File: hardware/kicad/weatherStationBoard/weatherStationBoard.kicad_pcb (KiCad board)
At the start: 2 copper layers, 27 x 13 mm, 3 parts, among them P1 USB_C_Plug_USB2.0

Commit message: power, 5vto3v, usb to serial
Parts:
- added 12k1: R_Small, Resistor_SMD:R_0805_2012Metric, F.Cu at (100.6, 12.9)
- added C1: 100nF, Capacitor_SMD:C_0805_2012Metric, F.Cu at (91.8, 12.9)
- added C10: 100nF, Capacitor_SMD:C_0805_2012Metric, F.Cu at (96.2, 24.9)
- added C2: 10uF, Capacitor_SMD:C_0805_2012Metric, F.Cu at (91.8, 15.9)
- added C3: 22pF, Capacitor_SMD:C_0805_2012Metric, F.Cu at (91.8, 18.9)
- added C4: 22pF, Capacitor_SMD:C_0805_2012Metric, F.Cu at (91.8, 21.9)
- added C5: 100nF, Capacitor_SMD:C_0805_2012Metric, F.Cu at (91.8, 24.9)
- added C6: 100nF, Capacitor_SMD:C_0805_2012Metric, F.Cu at (96.2, 12.9)
- added C7: 10uF, Capacitor_SMD:C_0805_2012Metric, F.Cu at (96.2, 15.9)
- added C8: 100nF, Capacitor_SMD:C_0805_2012Metric, F.Cu at (96.2, 18.9)
- added C9: 10uF, Capacitor_SMD:C_0805_2012Metric, F.Cu at (96.2, 21.9)
- added D1: LED, LED_SMD:LED_0805_2012Metric, F.Cu at (91.8, 44.0)
- added Q1: S8050, Package_TO_SOT_THT:TO-92_Inline, F.Cu at (100.0, 29.7)
- added Q2: S8050, Package_TO_SOT_THT:TO-92_Inline, F.Cu at (100.0, 35.5)
- added R2: 470R, Resistor_SMD:R_0805_2012Metric, F.Cu at (100.6, 15.8)
- added R3: 470R, Resistor_SMD:R_0805_2012Metric, F.Cu at (100.6, 18.8)
- added R4: 1k, Resistor_SMD:R_0805_2012Metric, F.Cu at (100.6, 21.7)
- added R5: 12k, Resistor_SMD:R_0805_2012Metric, F.Cu at (100.6, 24.7)
- added U1: ESP-12F, RF_Module:ESP-12E, F.Cu at (80.0, 24.1)
- added U2: CH340G, Package_SO:SOIC-16_3.9x9.9mm_P1.27mm, F.Cu at (93.8, 32.4)
- added U4: AMS1117-3.3, Package_TO_SOT_SMD:SOT-223-3_TabPin2, F.Cu at (75.3, 42.0)
- added Y1: Crystal_GND24_Small, Crystal:Crystal_SMD_3225-4Pin_3.2x2.5mm, F.Cu at (92.2, 40.3)
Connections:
- net USB_VBUS_5V renamed 5V
- P1 pad A6: unconnected-(P1-D+-PadA6) -> Net-(P1-D+)
- P1 pad A7: unconnected-(P1-D--PadA7) -> Net-(P1-D-)
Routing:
- net 5V: track 0.00 -> 16.5 mm
- net Net-(D2-A): track 0.00 -> 5.65 mm
- net GND: track 0.00 -> 5.33 mm
- added copper zone on B.Cu, net GND
- added copper zone on F.Cu, net GND

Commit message: PCB updated
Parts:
- Q1, Q2: footprint Package_TO_SOT_THT:TO-92_Inline -> Package_TO_SOT_SMD:SOT-23-3
- moved U1 80.3 mm to (151.5, 60.5), turned to -90 degrees
- moved 12k1 61.8 mm to (133.1, 65.5)
- moved C6 60.5 mm to (145.5, 48.0)
- moved R2 57.8 mm to (112.0, 72.5)
- moved C7 54.3 mm to (140.0, 48.0)
- moved Y1 49.0 mm to (130.4, 70.8)
- moved U4 45.0 mm to (118.5, 54.5)
- moved C3 44.9 mm to (126.1, 47.8)
- moved C5 44.9 mm to (126.1, 53.8)
- moved R3 44.9 mm to (135.0, 47.6)
- moved R5 44.9 mm to (135.0, 53.5)
- moved C4 44.9 mm to (126.1, 50.8)
- moved R4 44.9 mm to (135.0, 50.5)
- moved C10 44.9 mm to (130.6, 53.8)
- moved C8 44.9 mm to (130.6, 47.8)
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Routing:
- net 5V: track 16.5 -> 8.07 mm
- net Net-(D2-A): track 5.65 -> 0.00 mm
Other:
- board size 27 x 13 mm -> 61 x 31 mm

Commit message: Updated usb connector
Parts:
- added R6: 5k1, Resistor_SMD:R_0805_2012Metric, F.Cu at (139.9, 28.3)
- added R7: 10k, Resistor_SMD:R_0805_2012Metric, F.Cu at (139.9, 31.3)
- added S1: PTS645SM43SMTR92LFS, PTS645SM43SMTR92LFS:PTS645_SMT_, F.Cu at (144.5, 23.2)
- P1: footprint Connector_USB:USB_C_Receptacle_GCT_USB4085 -> Connector_USB:USB_C_Receptacle_XKB_U262-16XN-4BVC11
- moved P1 3.41 mm to (106.6, 61.3)
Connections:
- P1 pad A5: unconnected-(P1-CC-PadA5) -> Net-(P1-CC)
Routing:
- net 5V: track 8.07 -> 0.00 mm
- net GND: track 5.33 -> 0.00 mm

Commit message: board design prototype no periphery
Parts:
- removed 12k1: R_Small, Resistor_SMD:R_0805_2012Metric
- removed P1: USB_C_Plug_USB2.0, Connector_USB:USB_C_Receptacle_XKB_U262-16XN-4BVC11
- added J1: USB_C_Receptacle_USB2.0_16P, Connector_USB:USB_C_Receptacle_XKB_U262-16XN-4BVC11, F.Cu at (108.2, 61.0)
- added R8: 5k1, Resistor_SMD:R_0805_2012Metric, F.Cu at (108.2, 68.2)
- added R9: 12k, Resistor_SMD:R_0805_2012Metric, F.Cu at (135.6, 74.0)
- moved R2 48.5 mm to (160.5, 72.0), turned to 90 degrees
- moved S1 42.7 mm to (109.0, 47.0), turned to -90 degrees
- moved R6 38.4 mm to (111.2, 54.0), turned to 180 degrees
- moved R3 36.9 mm to (162.7, 72.0), turned to 90 degrees
- moved C5 23.5 mm to (149.2, 49.8)
- moved C4 22.9 mm to (121.8, 73.2)
- moved C3 21.5 mm to (126.8, 69.2), turned to -90 degrees
- moved D2 19.5 mm to (115.8, 70.8), turned to 0 degrees
- moved R4 19.0 mm to (116.0, 49.5), turned to 180 degrees
- moved C6 19.0 mm to (127.5, 54.0)
- moved Q1 16.2 mm to (139.6, 70.2), turned to 180 degrees
- moved C1 15.5 mm to (129.5, 56.5)
- moved R1 15.1 mm to (115.8, 68.0), turned to 0 degrees
- moved R7 14.1 mm to (134.2, 44.2), turned to -90 degrees
- moved C2 14.1 mm to (129.5, 58.8)
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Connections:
- S1 pad 1: unconnected-(S1-Pad1) -> /nRST
- S1 pad 3: unconnected-(S1-Pad3) -> GND
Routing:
- net /nRST: track 0.00 -> 94.1 mm, vias 0 -> 6
- net Net-(U2-RXD): track 0.00 -> 71.9 mm, vias 0 -> 2
- net Net-(U2-TXD): track 0.00 -> 71.4 mm, vias 0 -> 2
- net 3V3: track 0.00 -> 48.8 mm, vias 0 -> 2
- net 5V: track 0.00 -> 46.5 mm
- net Net-(U2-V3): track 0.00 -> 40.1 mm, vias 0 -> 4
- net /DTR: track 0.00 -> 40.0 mm, vias 0 -> 2
- net /GPIO0: track 0.00 -> 35.3 mm, vias 0 -> 4
- net /RTS: track 0.00 -> 22.4 mm, vias 0 -> 4
- net /XI: track 0.00 -> 15.4 mm, vias 0 -> 2
- net Net-(U2-UD-): track 0.00 -> 13.8 mm, vias 0 -> 2
- net Net-(U2-UD+): track 0.00 -> 12.8 mm, vias 0 -> 2
- net /XO: track 0.00 -> 12.8 mm
- net Net-(Q1-B): track 0.00 -> 10.9 mm
- net Net-(J1-CC2): track 0.00 -> 10.3 mm, vias 0 -> 2
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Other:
- board size 61 x 31 mm -> 68.5 x 41 mm

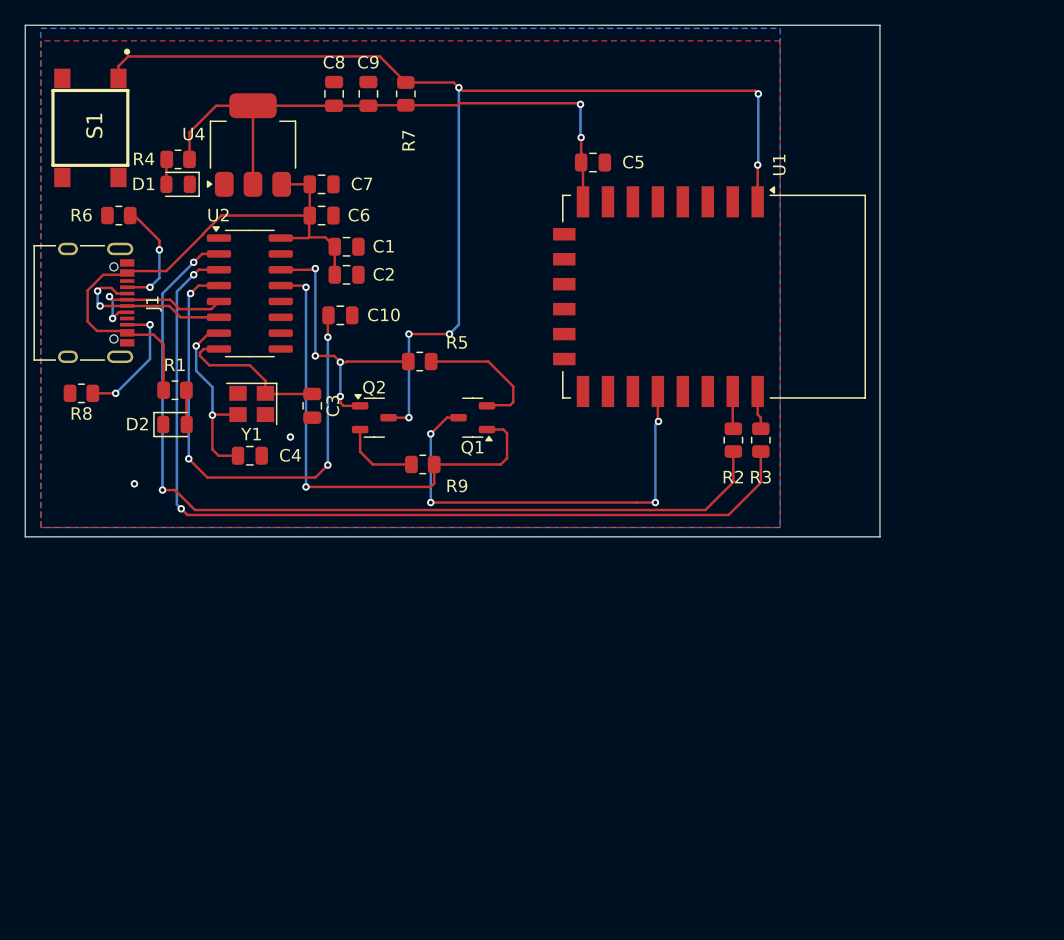
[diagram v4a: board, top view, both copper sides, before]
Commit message: Added BME680 Display-Connector and Mounting holes - 3D model of USB connector and Readme assets
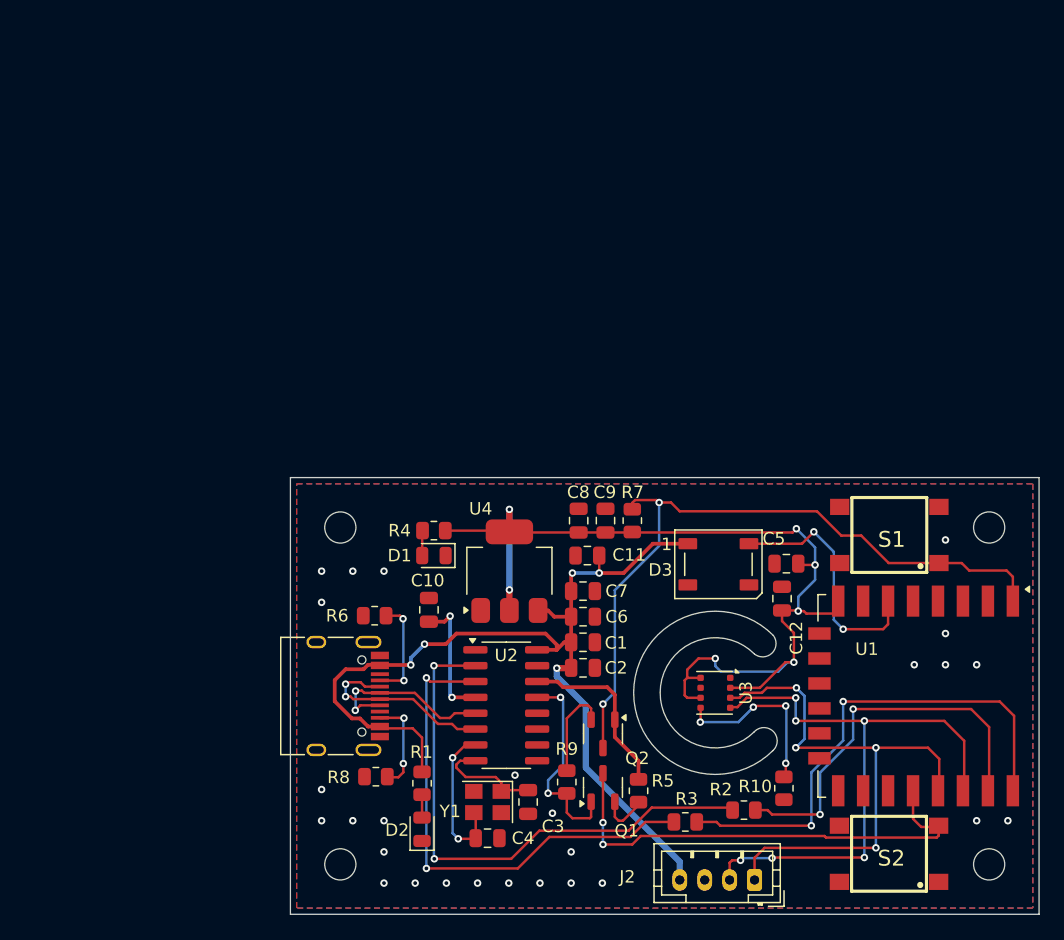
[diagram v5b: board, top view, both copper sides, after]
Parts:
- added C11: 100nF, Capacitor_SMD:C_0805_2012Metric, F.Cu at (148.8, 81.2)
- added C12: 100nF, Capacitor_SMD:C_0805_2012Metric, F.Cu at (164.4, 84.7)
- added D3: WS2812B, LED_SMD:LED_WS2812B_PLCC4_5.0x5.0mm_P3.2mm, F.Cu at (159.3, 82.0)
- added H1: MountingHole, MountingHole:MountingHole_2.5mm, F.Cu at (129.0, 79.0)
- added H2: MountingHole, MountingHole:MountingHole_2.5mm, F.Cu at (181.0, 79.0)
- added H3: MountingHole, MountingHole:MountingHole_2.5mm, F.Cu at (129.0, 106.0)
- added H4: MountingHole, MountingHole:MountingHole_2.5mm, F.Cu at (181.0, 106.0)
- added J2: Conn_01x04_Pin, Connector_JST:JST_PH_B4B-PH-K_1x04_P2.00mm_Vertical, F.Cu at (162.2, 107.2)
- added R10: 1k, Resistor_SMD:R_0805_2012Metric, F.Cu at (164.6, 99.9)
- added S2: PTS645SM43SMTR92LFS, PTS645SM43SMTR92LFS:PTS645_SMT_, F.Cu at (173.0, 105.2)
- added U3: BME680, Package_LGA:Bosch_LGA-8_3x3mm_P0.8mm_ClockwisePinNumbering, F.Cu at (159.1, 92.2)
- J1: footprint Connector_USB:USB_C_Receptacle_XKB_U262-16XN-4BVC11 -> Connector_USB:USB_C_Receptacle_HRO_TYPE-C-31-M-12
- moved S1 71.9 mm to (173.0, 79.6), turned to 180 degrees
- moved U4 39.9 mm to (142.6, 82.5)
- moved C8 39.4 mm to (148.1, 78.5)
- moved C9 39.1 mm to (150.2, 78.5)
- moved U2 38.9 mm to (142.3, 93.2)
- moved C7 38.8 mm to (148.4, 84.1)
- moved R8 38.7 mm to (131.8, 99.0)
- moved R7 38.7 mm to (152.4, 78.5)
- moved R5 38.6 mm to (152.9, 100.1), turned to 90 degrees
- moved C6 38.4 mm to (148.4, 86.2)
- moved R6 38.1 mm to (131.8, 86.1)
- moved D2 38.0 mm to (135.6, 103.2), turned to 90 degrees
- moved U1 38.0 mm to (179.4, 92.5)
- moved J1 37.3 mm to (128.1, 92.5)
- moved R1 37.2 mm to (135.6, 99.5), turned to -90 degrees
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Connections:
- net Net-(U2-UD+) renamed /USB_D+
- net Net-(U2-UD-) renamed /USB_D-
- S1 pad 2: unconnected-(S1-Pad2) -> GND
- U1 pad 19: unconnected-(U1-GPIO4-Pad19) -> /I2C_SDA
- U1 pad 20: unconnected-(U1-GPIO5-Pad20) -> /I2C_SCL
- U1 pad 6: unconnected-(U1-GPIO12-Pad6) -> /IO12
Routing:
- net /I2C_SCL: track 0.00 -> 49.9 mm, vias 0 -> 6
- net /I2C_SDA: track 0.00 -> 46.3 mm, vias 0 -> 4
- net /ESP TX: track 3.09 -> 41.5 mm, vias 0 -> 2
- net /nRST: track 94.1 -> 57.2 mm, vias 6 -> 2
- net 5V: track 46.5 -> 80.0 mm, vias 0 -> 5
- net Net-(U2-RXD): track 71.9 -> 40.7 mm
- net Net-(U2-V3): track 40.1 -> 10.3 mm, vias 4 -> 2
- net /ESP RX: track 3.01 -> 32.5 mm, vias 0 -> 2
- net 3V3: track 48.8 -> 76.9 mm, vias 2 -> 7
- net Net-(U2-TXD): track 71.4 -> 44.5 mm
- net /DTR: track 40.0 -> 17.2 mm
- net /IO12: track 0.00 -> 20.0 mm, vias 0 -> 2
- net Net-(U3-SDO): track 0.00 -> 14.3 mm, vias 0 -> 4
- net /RTS: track 22.4 -> 14.2 mm, vias 4 -> 0
- net Net-(Q1-B): track 10.9 -> 4.00 mm
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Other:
- board size 68.5 x 41 mm -> 60 x 35 mm

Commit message: Board&Case
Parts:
- removed J2: Conn_01x04_Pin, Connector_JST:JST_PH_B4B-PH-K_1x04_P2.00mm_Vertical
- added C13: 1uF, Capacitor_SMD:C_0805_2012Metric, F.Cu at (221.3, 103.7)
- added C14: 10uF, Capacitor_SMD:C_0805_2012Metric, F.Cu at (223.1, 112.5)
- added C15: 1uF, Capacitor_SMD:C_0805_2012Metric, F.Cu at (221.4, 101.0)
- added C16: 1uF, Capacitor_SMD:C_0805_2012Metric, F.Cu at (219.6, 123.0)
- added C17: 2uF, Capacitor_SMD:C_0805_2012Metric, F.Cu at (221.4, 126.0)
- added C18: 100nF, Capacitor_SMD:C_0805_2012Metric, F.Cu at (222.4, 124.0)
- added D4: 1N4148W, Diode_SMD:D_SOD-123, F.Cu at (223.1, 109.1)
- added J3: Conn_01x30_Pin, SSD1306:SSD1306_ribbon, F.Cu at (227.4, 113.5)
- added R11: 1k, Resistor_SMD:R_0805_2012Metric, F.Cu at (219.8, 109.8)
- added R12: 10k, Resistor_SMD:R_0805_2012Metric, F.Cu at (217.7, 109.8)
- added R13: 10k, Resistor_SMD:R_0805_2012Metric, F.Cu at (216.2, 118.9)
- added R14: 390K, Resistor_SMD:R_0805_2012Metric, F.Cu at (222.9, 121.2)
- D3: moved to B.Cu
- H1, H2, H3, H4: footprint MountingHole:MountingHole_2.5mm -> MountingHole:MountingHole_2.2mm_M2
- moved C5 56.4 mm to (215.0, 107.5), turned to 0 degrees
- moved D3 54.2 mm to (204.1, 112.5), turned to 90 degrees
- moved H4 52.6 mm to (228.5, 128.5)
- moved H2 51.3 mm to (228.5, 98.5)
- moved C12 39.2 mm to (192.9, 111.5), turned to 0 degrees
- moved S2 36.3 mm to (209.0, 100.8)
- moved U1 35.4 mm to (204.0, 118.0), turned to 180 degrees
- moved R10 33.4 mm to (192.8, 117.8)
- moved S1 33.3 mm to (198.8, 100.8)
- moved U3 33.1 mm to (184.5, 113.5)
- moved R3 30.1 mm to (176.8, 124.9)
- moved H3 29.8 mm to (148.5, 128.5)
- moved C1 29.7 mm to (169.4, 109.2)
- moved C10 29.7 mm to (157.1, 106.6)
- moved C11 29.7 mm to (169.8, 102.2)
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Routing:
- net 3V3: track 76.9 -> 142.5 mm, vias 7 -> 12
- net /GPIO0: track 38.1 -> 74.7 mm, vias 2 -> 6
- net /nRST: track 57.2 -> 86.7 mm, vias 2 -> 6
- net /ESP TX: track 41.5 -> 20.2 mm, vias 2 -> 0
- net 5V: track 80.0 -> 98.2 mm
- net /ESP RX: track 32.5 -> 17.0 mm, vias 2 -> 0
- net /IO12: track 20.0 -> 8.40 mm, vias 2 -> 1
- net Net-(D4-A): track 0.00 -> 9.21 mm
- net Net-(J3-Pin_3): track 0.00 -> 9.12 mm
- net Net-(J3-Pin_5): track 0.00 -> 8.74 mm
- net Net-(J3-Pin_27): track 0.00 -> 8.33 mm
- net Net-(J3-Pin_28): track 0.00 -> 8.10 mm
- net Net-(J3-Pin_2): track 0.00 -> 6.31 mm
- net Net-(J3-Pin_4): track 0.00 -> 5.87 mm
- net Net-(J3-Pin_29): track 0.00 -> 4.57 mm
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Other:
- board size 60 x 35 mm -> 85 x 35 mm
- board text added: "BOOT"
- board text added: "RESET"
- board text added: "d=1mm"

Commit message: Testpoints added
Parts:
- added TP1: 5V, TestPoint:TestPoint_Pad_D1.0mm, F.Cu at (169.7, 102.3)
- added TP10: GND, TestPoint:TestPoint_Pad_D1.0mm, F.Cu at (225.4, 125.9)
- added TP2: 3V3_BME, TestPoint:TestPoint_Pad_D1.0mm, F.Cu at (186.6, 109.2)
- added TP3: SDA, TestPoint:TestPoint_Pad_D1.0mm, F.Cu at (183.2, 117.5)
- added TP4: SCL, TestPoint:TestPoint_Pad_D1.0mm, F.Cu at (186.1, 117.5)
- added TP5: IO0, TestPoint:TestPoint_Pad_D1.0mm, F.Cu at (215.2, 98.5)
- added TP6: nRST, TestPoint:TestPoint_Pad_D1.0mm, F.Cu at (179.6, 98.1)
- added TP7: 3V3_LDO, TestPoint:TestPoint_Pad_D1.0mm, F.Cu at (176.2, 102.1)
- added TP8: 3V3_OLED, TestPoint:TestPoint_Pad_D1.0mm, F.Cu at (218.4, 106.2)
- added TP9: GND, TestPoint:TestPoint_Pad_D1.0mm, F.Cu at (151.7, 125.5)
- C11: moved to B.Cu
- moved C11 37.4 mm to (203.5, 118.5)
- moved D3 1.00 mm to (204.1, 113.5)
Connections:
- net Net-(U3-SDO) renamed /BME_SD0
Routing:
- net 5V: track 98.2 -> 101.1 mm
- net /nRST: track 86.7 -> 84.8 mm, vias 6 -> 7
- net 3V3: track 142.5 -> 141.0 mm
- net /IO12: track 8.40 -> 9.40 mm
- net GND: vias 66 -> 65
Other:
- board text added: "5V"

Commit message: REV1 WeatherStationBoard
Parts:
- moved TP10 41.7 mm to (186.9, 109.8)
- moved TP7 18.1 mm to (158.6, 98.1)
- moved C10 4.81 mm to (156.6, 111.4)
- moved TP2 4.02 mm to (182.6, 109.5)
- moved C16 3.62 mm to (223.1, 121.9), turned to 180 degrees
- moved C15 2.55 mm to (223.1, 103.0)
- moved C13 2.30 mm to (223.1, 105.2)
- moved TP6 2.08 mm to (177.5, 98.5)
- moved TP9 1.99 mm to (150.2, 124.3)
- moved C17 1.65 mm to (223.1, 126.0)
- moved TP3 1.56 mm to (184.8, 117.7)
- moved R6 1.43 mm to (151.5, 106.4)
- moved R14 1.31 mm to (223.1, 119.9)
- moved TP4 0.85 mm to (186.9, 117.4)
- moved C18 0.65 mm to (223.1, 124.0)
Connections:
- J3 pad 29: Net-(J3-Pin_29) -> GND
- J3 pad 30: Net-(J3-Pin_29) -> GND
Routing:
- net 3V3: track 141.0 -> 154.1 mm
- net Net-(U2-V3): track 10.3 -> 4.80 mm, vias 2 -> 0
- net Net-(J3-Pin_27): track 8.33 -> 3.54 mm
- net Net-(J3-Pin_29): track 4.57 -> 0.00 mm
- net /I2C_SDA: track 50.2 -> 54.5 mm
- net Net-(U2-RXD): track 39.4 -> 36.1 mm
- net /I2C_SCL: track 52.2 -> 55.4 mm
- net 5V: track 101.1 -> 104.2 mm
- net Net-(J3-Pin_3): track 9.12 -> 6.05 mm
- net Net-(J3-Pin_5): track 8.74 -> 5.76 mm
- net Net-(J3-Pin_2): track 6.31 -> 3.86 mm
- net Net-(J3-Pin_4): track 5.87 -> 3.50 mm
- net /nRST: track 84.8 -> 86.8 mm, vias 7 -> 6
- net Net-(J3-Pin_28): track 8.10 -> 6.34 mm
- net /GPIO0: track 74.7 -> 76.1 mm
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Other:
- outline, holes or cut-outs redrawn
- board text added: "3V3"
- board text added: "GND"
- board text added: "SCL"
- board text added: "SDA"
- board text added: "nRST"
